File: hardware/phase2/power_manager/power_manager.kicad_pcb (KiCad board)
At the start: 4 copper layers, 40 x 40 mm, 84 parts, among them J1 1725656, J2 Conn_02x04_Odd_Even, J3 S2B-PH-K-SLFSN, J4 OSTVN04A150, J5 10118194-0001LF, U1 LTC3586EUFE-PBF, U2 TPS60403DBVR, U3 TPS73225DBVR, U4 TPS72325DBVR

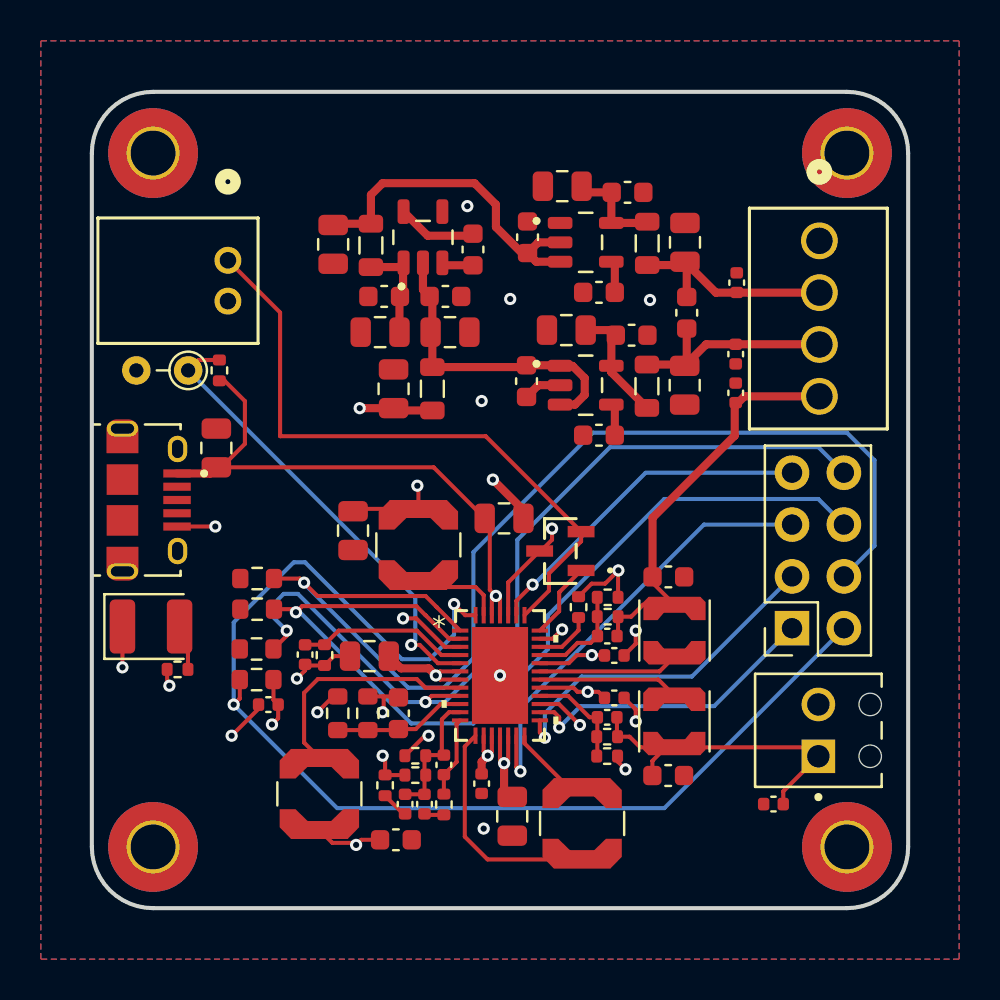
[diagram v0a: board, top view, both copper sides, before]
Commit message: Update power path track widths
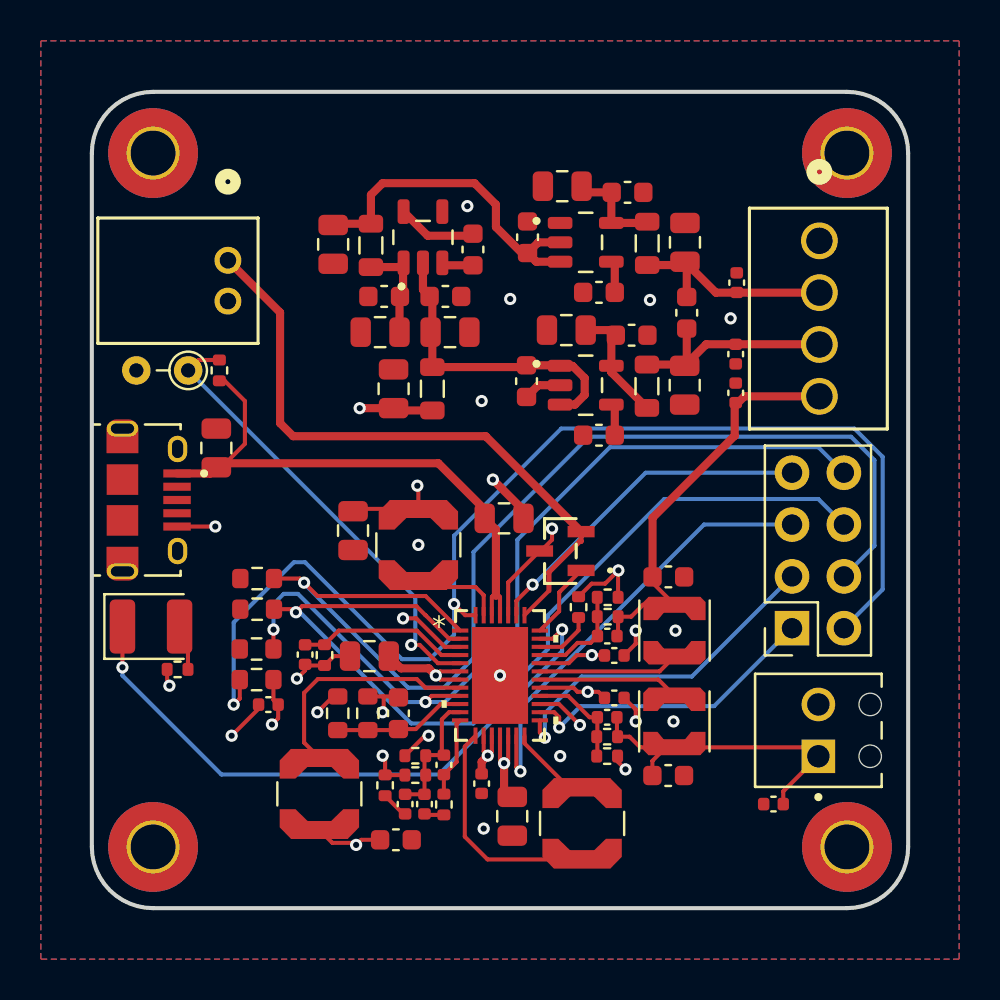
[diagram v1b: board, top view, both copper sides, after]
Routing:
- net /NFAULT: track 58.3 -> 58.9 mm
- net /MODE: track 43.2 -> 42.6 mm
- net /PWRIN: track 28.1 -> 28.5 mm, vias 1 -> 0
- net GND: vias 16 -> 21

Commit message: Remove all DRC
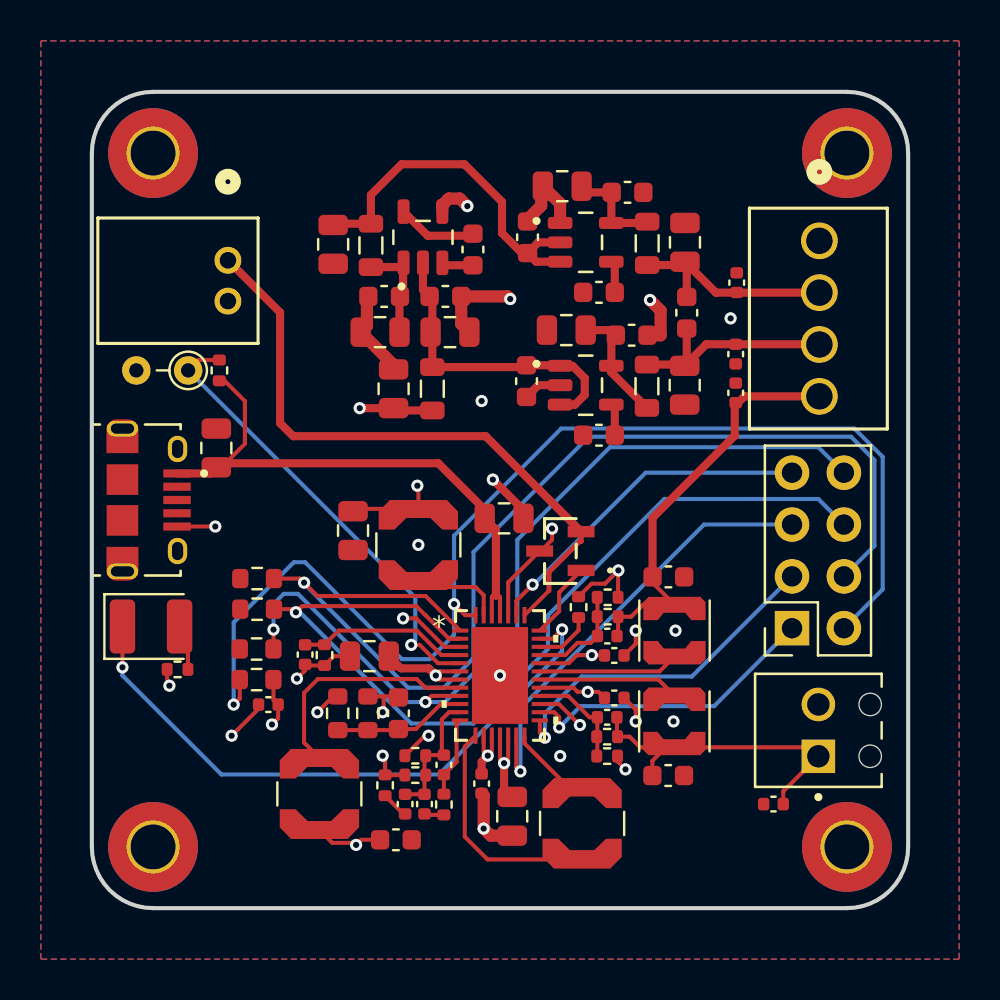
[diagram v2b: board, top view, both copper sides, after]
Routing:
- net GND: track 22.0 -> 42.7 mm
- net -5V: track 16.8 -> 17.9 mm
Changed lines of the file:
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@@
+	)
+	(segment
+		(start 171.35 86.35)
+		(end 171.35 86.25)
+		(width 0.6)
+		(layer "F.Cu")
+		(net 1)
 	)
 	(segment
@@
 	)
 	(segment
+		(start 169.2 114.477598)
+		(end 169.1 114.377598)
+		(width 0.6)
+		(layer "F.Cu")
+		(net 1)
+	)
+	(segment
+		(start 169.2 116.1)
+		(end 169.2 114.477598)
+		(width 0.6)
+		(layer "F.Cu")
+		(net 1)
+	)
+	(segment
 		(start 161.825 109.625)
 		(end 161.05 110.4)
@@
 	)
 	(segment
+		(start 167.175 85.87)
+		(end 167.175 85.545)
+		(width 0.6)
+		(layer "F.Cu")
+		(net 1)
+	)
+	(segment
 		(start 176.08 109.697598)
 		(end 176.65 110.267598)
@@
 	)
 	(segment
+		(start 168.03 85.23)
+		(end 168.4 85.6)
+		(width 0.6)
+		(layer "F.Cu")
+		(net 1)
+	)
+	(segment
 		(start 165.34 112.53)
 		(end 166.32 111.55)
@@
 	)
 	(segment
+		(start 172.02 85.58)
+		(end 172.02 84.705)
+		(width 0.6)
+		(layer "F.Cu")
+		(net 1)
+	)
+	(segment
+		(start 169.547598 116.447598)
+		(end 169.2 116.1)
+		(width 0.6)
+		(layer "F.Cu")
+		(net 1)
+	)
+	(segment
 		(start 173.85 104.74)
 		(end 174.49 104.1)
@@
 	)
 	(segment
+		(start 167.175 85.545)
+		(end 167.49 85.23)
+		(width 0.6)
+		(layer "F.Cu")
+		(net 1)
+	)
+	(segment
 		(start 171.3 94.95)
 		(end 171.875 94.375)
@@
 	)
 	(segment
+		(start 172.945 85.47)
+		(end 172.1 84.625)
+		(width 0.6)
+		(layer "F.Cu")
+		(net 1)
+	)
+	(segment
 		(start 160.45 108.055)
 		(end 160.45 108.35)
@@
 	)
 	(segment
+		(start 167.49 85.23)
+		(end 168.03 85.23)
+		(width 0.6)
+		(layer "F.Cu")
+		(net 1)
+	)
+	(segment
+		(start 171.35 86.25)
+		(end 172.02 85.58)
+		(width 0.6)
+		(layer "F.Cu")
+		(net 1)
+	)
+	(segment
+		(start 177.23 91.93)
+		(end 177.87 91.93)
+		(width 0.6)
+		(layer "F.Cu")
+		(net 1)
+	)
+	(segment
+		(start 177.87 90.72)
+		(end 177.35 90.2)
+		(width 0.6)
+		(layer "F.Cu")
+		(net 1)
+	)
+	(segment
 		(start 175.76 112.547598)
 		(end 175.76 112.81)
@@
 	)
 	(segment
+		(start 172.02 84.705)
+		(end 172.1 84.625)
+		(width 0.6)
+		(layer "F.Cu")
+		(net 1)
+	)
+	(segment
 		(start 176.65 107.047598)
 		(end 176.08 107.617598)
@@
 	)
 	(segment
+		(start 164.785 93.385)
+		(end 163.175 91.775)
+		(width 0.6)
+		(layer "F.Cu")
+		(net 1)
+	)
+	(segment
 		(start 175.785 103.465)
 		(end 175.8 103.45)
@@
 	)
 	(segment
+		(start 163.48 90.095)
+		(end 163.55 90.025)
+		(width 0.6)
+		(layer "F.Cu")
+		(net 1)
+	)
+	(segment
+		(start 168.1 90.025)
+		(end 170.375 90.025)
+		(width 0.6)
+		(layer "F.Cu")
+		(net 1)
+	)
+	(segment
 		(start 160.45 108.35)
 		(end 160.05 108.75)
@@
 	)
 	(segment
+		(start 168.1 90.025)
+		(end 168.1 91.375)
+		(width 0.6)
+		(layer "F.Cu")
+		(net 1)
+	)
+	(segment
+		(start 168.1 91.375)
+		(end 168.5 91.775)
+		(width 0.6)
+		(layer "F.Cu")
+		(net 1)
+	)
+	(segment
+		(start 163.175 91.775)
+		(end 163.48 91.47)
+		(width 0.6)
+		(layer "F.Cu")
+		(net 1)
+	)
+	(segment
+		(start 170.375 90.025)
+		(end 170.5 90.15)
+		(width 0.6)
+		(layer "F.Cu")
+		(net 1)
+	)
+	(segment
+		(start 172.945 86.425)
+		(end 172.945 85.47)
+		(width 0.6)
+		(layer "F.Cu")
+		(net 1)
+	)
+	(segment
 		(start 162.65 107.65)
 		(end 161.86 107.65)
@@
 	)
 	(segment
+		(start 164.785 93.6)
+		(end 164.785 93.385)
+		(width 0.6)
+		(layer "F.Cu")
+		(net 1)
+	)
+	(segment
 		(start 160.505 108.11)
 		(end 160.45 108.055)
@@
 	)
 	(segment
+		(start 163.48 91.47)
+		(end 163.48 90.095)
+		(width 0.6)
+		(layer "F.Cu")
+		(net 1)
+	)
+	(segment
+		(start 170.6 116.447598)
+		(end 169.547598 116.447598)
+		(width 0.6)
+		(layer "F.Cu")
+		(net 1)
+	)
+	(segment
 		(start 158.17 110.23)
 		(end 156.85 111.55)
@@
 	)
 	(segment
+		(start 177.87 91.93)
+		(end 177.87 90.72)
+		(width 0.6)
+		(layer "F.Cu")
+		(net 1)
+	)
+	(segment
+		(start 177.225 91.925)
+		(end 177.23 91.93)
+		(width 0.6)
+		(layer "F.Cu")
+		(net 1)
+	)
+	(segment
 		(start 161.86 107.65)
 		(end 161.4 108.11)
@@
 	)
 	(segment
-		(start 163.675 85.05)
-		(end 164.25 84.475)
+		(start 170.1 86.925)
+		(end 171.075 87.9)
+		(width 0.4)
+		(layer "F.Cu")
+		(net 14)
+	)
+	(segment
+		(start 168.26 83.55)
+		(end 170.1 85.39)
+		(width 0.4)
+		(layer "F.Cu")
+		(net 14)
+	)
+	(segment
+		(start 170.1 85.39)
+		(end 170.1 86.925)
 		(width 0.4)
 		(layer "F.Cu")
@@
 	)
 	(segment
+		(start 172.945 88.325)
+		(end 171.775 88.325)
+		(width 0.4)
+		(layer "F.Cu")
+		(net 14)
+	)
+	(segment
+		(start 172.945 87.375)
+		(end 171.875 87.375)
+		(width 0.4)
+		(layer "F.Cu")
+		(net 14)
+	)
+	(segment
 		(start 171.075 87.9)
 		(end 171.35 87.9)
@@
 	)
 	(segment
-		(start 172.945 88.325)
-		(end 171.775 88.325)
-		(width 0.4)
-		(layer "F.Cu")
-		(net 14)
-	)
-	(segment
-		(start 172.945 87.375)
-		(end 171.875 87.375)
-		(width 0.4)
-		(layer "F.Cu")
-		(net 14)
-	)
-	(segment
-		(start 169.8 85.525)
-		(end 169.8 86.625)
-		(width 0.4)
-		(layer "F.Cu")
-		(net 14)
-	)
-	(segment
-		(start 169.8 86.625)
-		(end 171.075 87.9)
-		(width 0.4)
-		(layer "F.Cu")
-		(net 14)
-	)
-	(segment
 		(start 163.675 86.4625)
 		(end 163.675 85.05)
@@
 	)
 	(segment
-		(start 168.75 84.475)
-		(end 169.8 85.525)
+		(start 165.175 83.55)
+		(end 168.26 83.55)
 		(width 0.4)
 		(layer "F.Cu")
@@
 	)
 	(segment
-		(start 164.25 84.475)
-		(end 168.75 84.475)
-		(width 0.4)
-		(layer "F.Cu")
+		(start 163.675 85.05)
+		(end 165.175 83.55)
+		(width 0.4)
+		(layer "F.Cu")

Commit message: Add changes based on bruno's suggestions for thermal releif
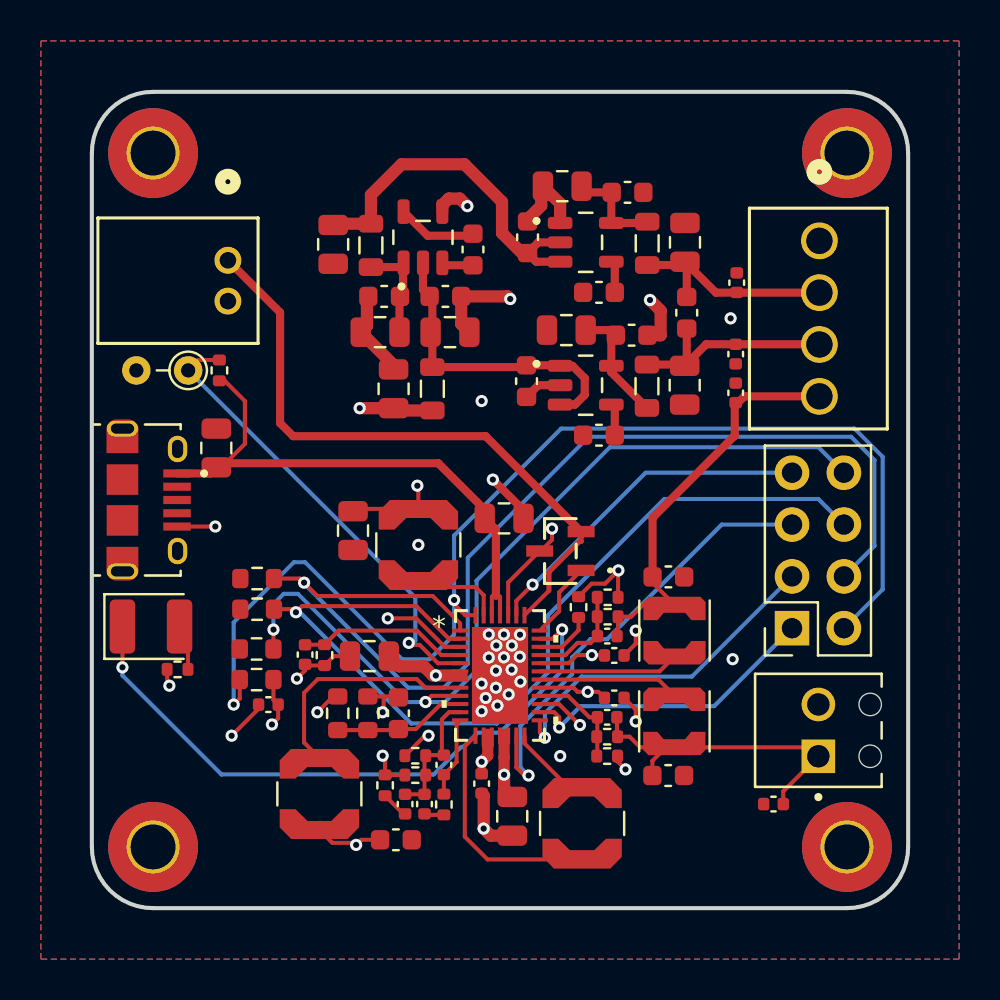
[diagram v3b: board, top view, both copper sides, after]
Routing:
- net /VIN1: track 87.5 -> 85.2 mm
- net +3V3HC: track 13.5 -> 12.0 mm
- net +5V: track 46.7 -> 45.4 mm
- net /EN3: track 22.0 -> 22.8 mm
- net /ILIM1: track 45.1 -> 45.8 mm
- net /NCHRG: track 30.8 -> 31.4 mm
- net GND: vias 21 -> 36

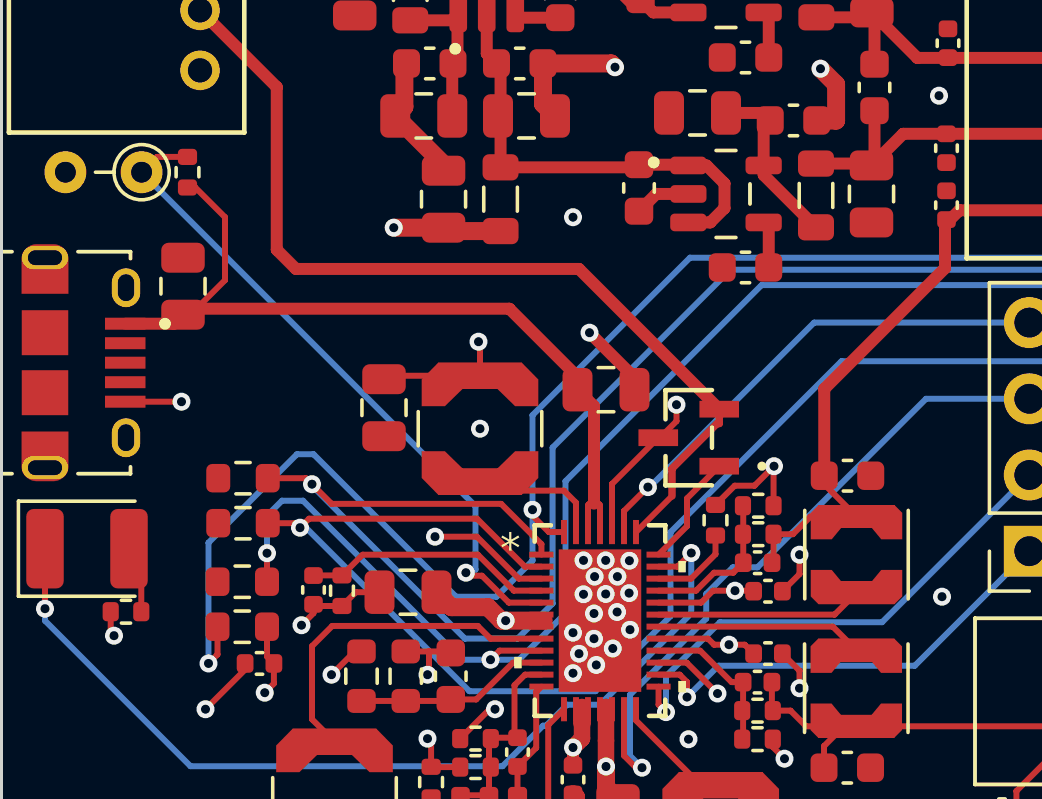
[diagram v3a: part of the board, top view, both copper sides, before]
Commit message: Added ECG portions to the final, corrected -5 points
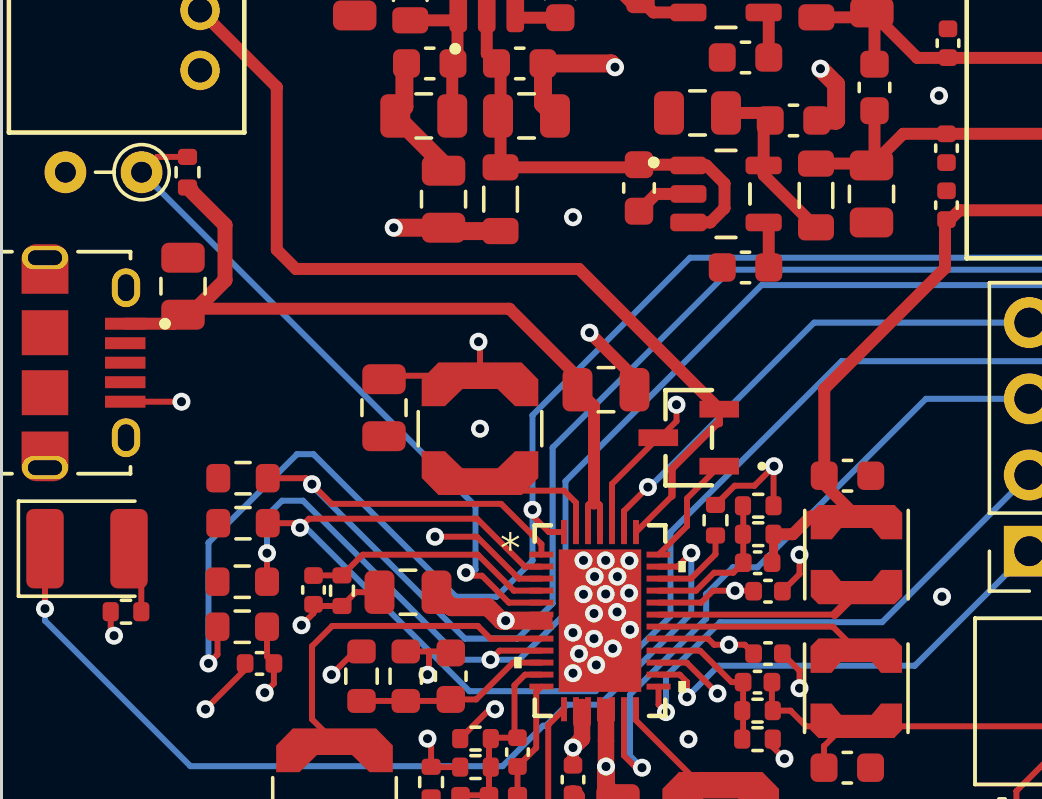
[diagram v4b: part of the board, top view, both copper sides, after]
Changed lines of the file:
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@@
-	)
-	(segment
-		(start 157.5 95.15)
-		(end 156.51 94.16)
-		(width 0.2)
-		(layer "F.Cu")
-		(net 2)
 	)
 	(segment
@@
 	)
 	(segment
+		(start 157.5 97.25)
+		(end 157.5 95.41)
+		(width 0.5)
+		(layer "F.Cu")
+		(net 2)
+	)
+	(segment
+		(start 157.5 95.41)
+		(end 156.25 94.16)
+		(width 0.5)
+		(layer "F.Cu")
+		(net 2)
+	)
+	(segment
 		(start 154.175 98.7)
 		(end 155.8 98.7)
@@
 	)
 	(segment
-		(start 157.5 97.25)
-		(end 157.5 95.15)
-		(width 0.2)
-		(layer "F.Cu")
-		(net 2)
-	)
-	(segment
 		(start 156.35 98.4)
 		(end 157.5 97.25)
-		(width 0.2)
+		(width 0.5)
 		(layer "F.Cu")
 		(net 2)
@@
 		(start 177.82 108.397598)
 		(end 178.55 107.667598)
-		(width 0.2)
+		(width 0.3)
 		(layer "F.Cu")
 		(net 48)
@@
 		(start 175.785 106.617598)
 		(end 175.735 106.667598)
-		(width 0.2)
+		(width 0.3)
 		(layer "F.Cu")
 		(net 56)
@@
 		(start 177.475 103.767598)
 		(end 177.475 104.052598)
-		(width 0.2)
+		(width 0.4)
 		(layer "F.Cu")
 		(net 56)
@@
 		(start 175.785 105.717598)
 		(end 175.785 106.617598)
-		(width 0.2)
+		(width 0.3)
 		(layer "F.Cu")
 		(net 56)
@@
 		(start 177.475 104.052598)
 		(end 178.55 105.127598)
-		(width 0.2)
+		(width 0.4)
 		(layer "F.Cu")
 		(net 56)
@@
 		(start 175.785 105.717598)
 		(end 176.43 105.717598)
-		(width 0.2)
+		(width 0.4)
 		(layer "F.Cu")
 		(net 56)
@@
 		(start 176.43 105.717598)
 		(end 177.02 105.127598)
-		(width 0.2)
+		(width 0.4)
 		(layer "F.Cu")
 		(net 56)
@@
 		(start 177.02 105.127598)
 		(end 178.55 105.127598)
-		(width 0.2)
+		(width 0.4)
 		(layer "F.Cu")
 		(net 56)
